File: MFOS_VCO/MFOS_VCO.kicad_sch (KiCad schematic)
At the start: 115 parts, among them J1 PWR, J10 AudioJack2, J11 AudioJack2, J12 Conn_01x01, J13 Conn_01x01, J14 Conn_01x01, J15 Conn_01x01, J16 Conn_01x01, J17 Conn_01x01, J18 Conn_01x01, J19 Conn_01x01, J2 AudioJack2, J21 Conn_01x01, J23 Conn_01x01, J25 Conn_01x01, J3 AudioJack2, J4 AudioJack2, J5 AudioJack2, J6 AudioJack2, J7 AudioJack2, J8 AudioJack2, J9 AudioJack2, Q1 PN4391, U1 OP275, U2 TL072, U3 SSM2212, U4 TL074, U5 LM13700, U6 TL072, U7 TL071

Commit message: Reviewed BOM
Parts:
- C12: value 0.1u -> 1u; symbol Device:C_Polarized -> dhk:C_Tantalum
- C13: symbol Device:C_Polarized -> dhk:C_Tantalum
- C6: symbol Device:C -> dhk:R_Potentiometer_Trim_Top
- D1, D2, D3, D4, D5, D6, D7, D8: value D -> 1N914; footprint (none) -> Diode_THT:D_DO-35_SOD27_P7.62mm_Horizontal; symbol Device:D -> Diode:1N914
- J1, J12, J13, J14, J15, J16, J17, J18, J19, J21, J23, J25: now left out of the parts list
- J10, J11, J2, J3, J4, J5, J6, J7, J8, J9: symbol Connector:AudioJack2 -> Connector:Jack-DC
- R11, R16, R5, R59, R60, R64, R7: symbol Device:R_Potentiometer -> dhk:R_Potentiometer_Trim_Top
- R24: value 2k -> 1.5k
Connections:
- net CV1: now also J2.2; no longer J2.T
- net CV2: now also J3.2; no longer J3.T
- net CV3: now also J4.2; no longer J4.T
- net GND: now also J10.1, J11.1, J8.1, J9.1; no longer J10.S, J11.S, J8.S, J9.S
- net LIN: now also J5.2; no longer J5.T
- net PWM: now also J6.2; no longer J6.T
- net RAW: now also C6.3; no longer C6.2
- net RMP: now also J11.2; no longer J11.T
- net SIN: now also J9.2; no longer J9.T
- net SQR: now also J10.2; no longer J10.T
- net SYNC: now also J7.2; no longer J7.T
- net TRI: now also J8.2; no longer J8.T

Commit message: Designs adapted for BOM
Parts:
- C1: value 0.1u -> 0.1uF
- C10, C7: value 10u -> 10uF
- C12, C13: value 1u -> 1uF
- C14: value 0.002u -> 0.002uF
- C15, C16, C2, C8: value .1u -> 0.1uF
- C17, C3: value 100p -> 100pF
- C18: value 4.7p -> 4.7pF
- C4: value 10p -> 10pF
- C5: value 0.001u -> 0.001uF
- C6: value 0.005u -> .005uF; symbol dhk:R_Potentiometer_Trim_Top -> dhk:C_Polystyrene
- J10, J11, J2, J3, J4, J5, J6, J7, J8, J9: value AudioJack2 -> Jack-DC
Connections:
- net RAW: now also C6.2; no longer C6.3

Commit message: yeah yeah
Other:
- moved on the sheet: C1, C12, C13, C14, C15, C16, C2, C4, D2, D3, D4, D5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

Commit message: Final changes
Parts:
- removed C1, C15, C16, C2: 0.1uF, symbol Device:C
- removed C12, C13: 1uF, symbol dhk:C_Tantalum
- removed C14: 0.002uF, symbol Device:C
- removed C4: 10pF, symbol Device:C
- removed D2, D3, D4, D5, D6, D7: 1N914, Diode_THT:D_DO-35_SOD27_P7.62mm_Horizontal, symbol Diode:1N914
- removed R1, R12, R13, R25, R32, R35, R40: 10k, symbol Device:R
- removed R14, R21, R48: 20k, symbol Device:R
- removed R20: 47k, symbol Device:R
- removed R22, R26, R49, R51: 1k, symbol Device:R
- removed R29, R44, R6, R67: 100k, symbol Device:R
- removed R36, R52: 4.7k, symbol Device:R
- removed R39: 100k, symbol Device:R_Potentiometer
- removed R41: 3k, symbol Device:R
- removed R45: 1M, symbol Device:R
- removed R5, R7: 10k, symbol dhk:R_Potentiometer_Trim_Top
- removed R53: 130k, symbol Device:R
- removed R59: 1M, symbol dhk:R_Potentiometer_Trim_Top
- removed R60, R64: 100k, symbol dhk:R_Potentiometer_Trim_Top
- removed R61: 470k, symbol Device:R
- removed R68: 10M, symbol Device:R
- removed unit 1 of U4
- removed unit 4 of U4
- removed unit 3 of U4
- removed unit 2 of U4
- removed unit 2 of U5
- removed unit 1 of U5
- removed unit 3 of U5
- removed unit 4 of U5
- removed unit 2 of U6
- removed unit 1 of U6
- removed U7: TL071, symbol Amplifier_Operational:TL071
- added J20: Jack-DC, symbol Connector:Jack-DC
- added J22: Conn_01x01, symbol Connector_Generic:Conn_01x01
- added R27: 100k, symbol Device:R
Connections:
- net at C19.1, R10.2, R15.2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: now also R27.2
- net R2P1: now reaches R2.1, R71.2
- net R2P2: now reaches R10.1, R2.2
- net R3P1: now reaches R3.1, R56.2
- net R2P3: now reaches R2.3, R65.1
- net R3P3: now reaches R3.3, R57.1
- net R3P2: now reaches R3.2, R8.1
- new net CV4: J20.2, J22.1 (Pin_1), R27.1
- no-connect marks 14 -> 7
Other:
- moved on the sheet: J15, J16, J5, J6

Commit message: Lots of headway
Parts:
- removed J1: PWR, symbol Connector_Generic:Conn_02x08_Odd_Even
- added J1: Conn_02x05_Odd_Even, Connector_IDC:IDC-Header_2x05_P2.54mm_Vertical, symbol Connector_Generic:Conn_02x05_Odd_Even
- added J24, J26: Conn_01x03, Connector_PinHeader_2.54mm:PinHeader_1x03_P2.54mm_Vertical, symbol Connector_Generic:Conn_01x03
- C10, C7: footprint (none) -> Capacitor_THT:CP_Radial_D4.0mm_P1.50mm
- C17, C18, C19, C3, C5: footprint (none) -> Capacitor_THT:C_Disc_D3.4mm_W2.1mm_P2.50mm
- C6: footprint (none) -> Capacitor_THT:C_Axial_L12.0mm_D6.5mm_P15.00mm_Horizontal
- C8: footprint (none) -> Capacitor_THT:C_Disc_D5.0mm_W2.5mm_P2.50mm
- J12, J13, J14, J15, J16, J17, J18, J19, J21, J22, J23, J25: footprint (none) -> Connector_Pin:Pin_D1.0mm_L10.0mm_LooseFit
- Q1: footprint (none) -> Package_TO_SOT_THT:TO-92
- R10, R11, R15, R16, R17, R18, R19, R23, R24, R27, R28, R30, R31, R34, R42, R46, R47, R50, R56, R57, R65, R66, R69, R70, R71, R8, R9: footprint (none) -> Resistor_THT:R_Axial_DIN0207_L6.3mm_D2.5mm_P7.62mm_Horizontal
- U1, U2, U6: footprint (none) -> Package_DIP:DIP-8_W7.62mm_Socket_LongPads
- U3: footprint (none) -> Package_SO:SOIC-8_3.9x4.9mm_P1.27mm
- U4: footprint (none) -> Package_DIP:DIP-14_W7.62mm_Socket_LongPads
- U5: footprint (none) -> Package_SO:SOIC-16_3.9x9.9mm_P1.27mm
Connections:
- net +12V: now also J1.10 (Pin_10), J1.9 (Pin_9)
- net -12V: now also J1.1 (Pin_1), J1.2 (Pin_2)
- net GND: now also J1.3 (Pin_3), J1.4 (Pin_4), J1.5 (Pin_5), J1.6 (Pin_6), J1.7 (Pin_7), J1.8 (Pin_8)
- net R2P1: now also J26.1 (Pin_1)
- net R2P2: now also J26.2 (Pin_2)
- net R2P3: now also J26.3 (Pin_3)
- net R3P1: now also J24.1 (Pin_1)
- net R3P2: now also J24.2 (Pin_2)
- net R3P3: now also J24.3 (Pin_3)

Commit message: Laying out
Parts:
- removed J12, J13, J14, J22: Conn_01x01, Connector_Pin:Pin_D1.0mm_L10.0mm_LooseFit, symbol Connector_Generic:Conn_01x01
- added J12: Conn_01x04, Connector_PinHeader_2.54mm:PinHeader_1x04_P2.54mm_Vertical, symbol Connector_Generic:Conn_01x04
- R11, R16: footprint Resistor_THT:R_Axial_DIN0207_L6.3mm_D2.5mm_P7.62mm_Horizontal -> Potentiometer_THT:Potentiometer_Bourns_3339P_Vertical
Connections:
- net CV1: now also J12.1 (Pin_1)
- net CV2: now also J12.2 (Pin_2)
- net CV3: now also J12.3 (Pin_3)
- net CV4: now also J12.4 (Pin_4)
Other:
- moved on the sheet: J2, J20, J3, J4

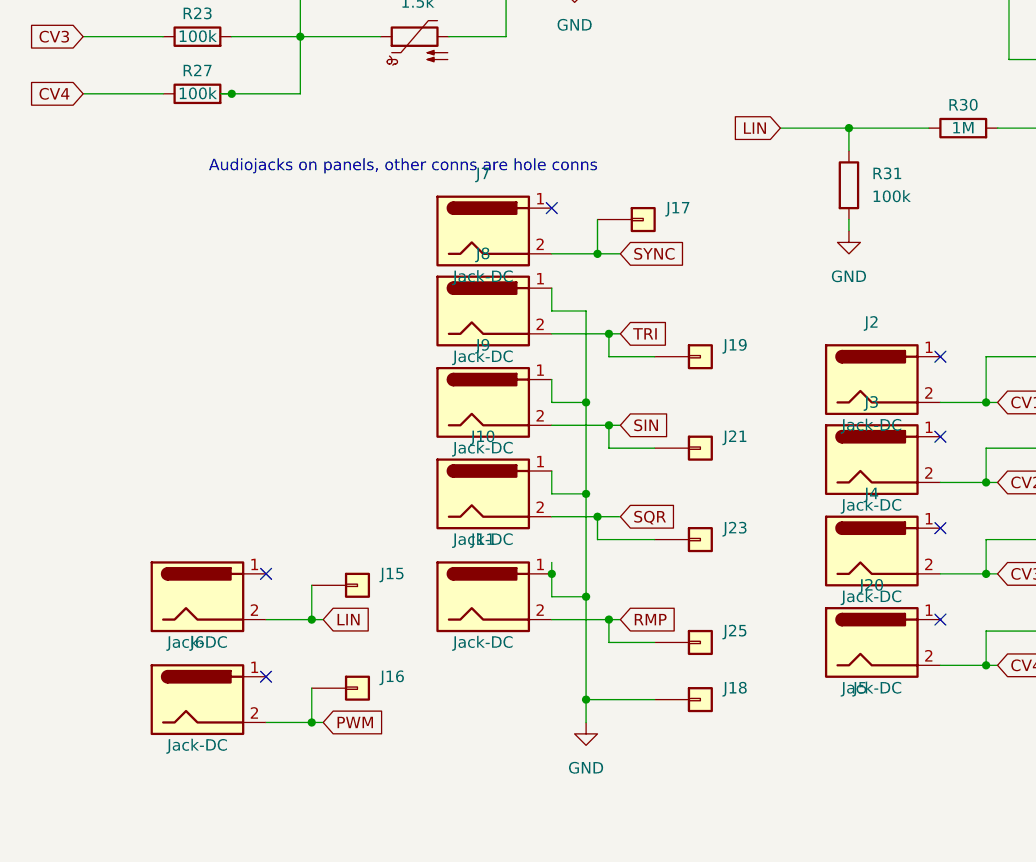
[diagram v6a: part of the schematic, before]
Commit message: Laid out last part of sheet 1
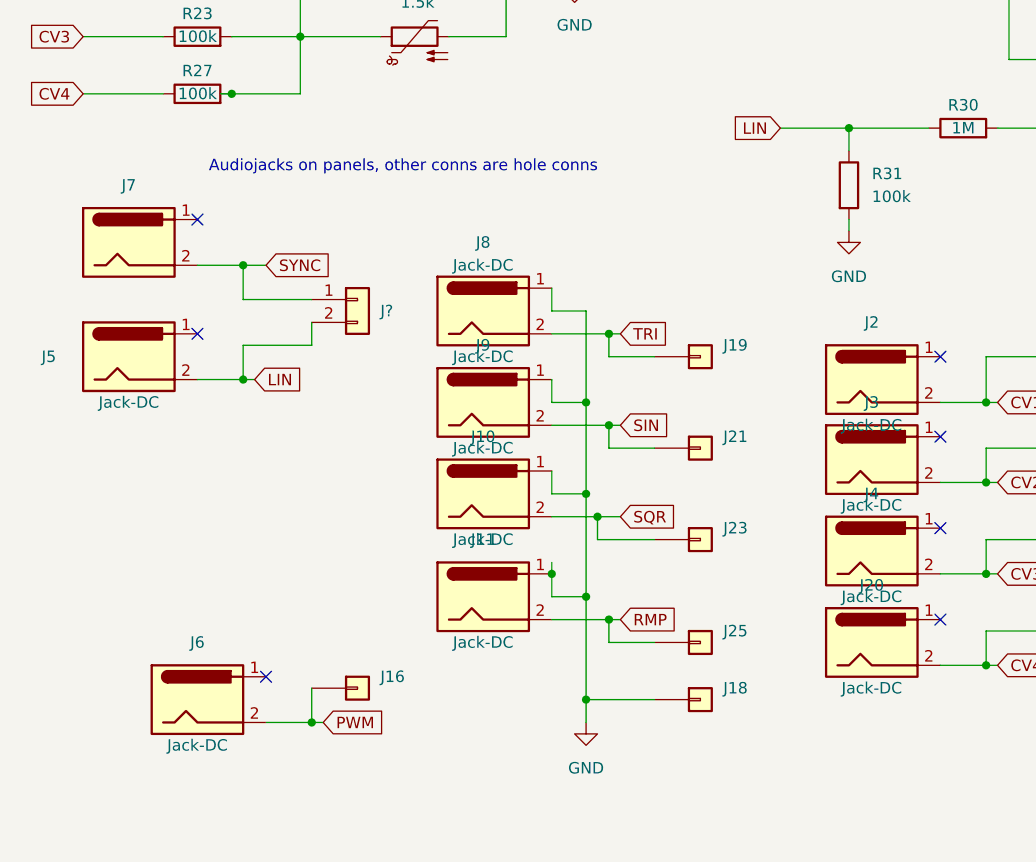
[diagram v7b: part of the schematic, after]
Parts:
- removed J15, J17: Conn_01x01, Connector_Pin:Pin_D1.0mm_L10.0mm_LooseFit, symbol Connector_Generic:Conn_01x01
- added J?: Conn_01x02, symbol Connector_Generic:Conn_01x02
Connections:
- net LIN: now also J?.2 (Pin_2)
- net SYNC: now also J?.1 (Pin_1)
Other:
- moved on the sheet: J5, J7
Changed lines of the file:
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@@
   (junction (at 55.88 34.29) (diameter 0) (color 0 0 0 0)
   )
-  (junction (at 90.17 128.27) (diameter 0) (color 0 0 0 0)
+  (junction (at 50.8 129.54) (diameter 0) (color 0 0 0 0)
   )
   (junction (at 123.19 19.05) (diameter 0) (color 0 0 0 0)
@@
   (junction (at 133.35 153.67) (diameter 0) (color 0 0 0 0)
   )
-  (junction (at 58.42 168.91) (diameter 0) (color 0 0 0 0)
+  (junction (at 50.8 142.24) (diameter 0) (color 0 0 0 0)
   )
   (junction (at 205.74 120.65) (diameter 0) (color 0 0 0 0)
@@
   )
   (no_connect (at 128.27 168.91))
-  (no_connect (at 85.09 123.19))
+  (no_connect (at 45.72 124.46))
   (no_connect (at 53.34 175.26))
-  (no_connect (at 53.34 163.83))
+  (no_connect (at 45.72 137.16))
   (no_connect (at 128.27 139.7))
   (no_connect (at 128.27 158.75))
@@
     (stroke (width 0) (type default) (color 0 0 0 0))
   )
+  (wire (pts (xy 58.42 138.43) (xy 58.42 135.89))
+    (stroke (width 0) (type default) (color 0 0 0 0))
+  )
   (wire (pts (xy 91.44 171.45) (xy 96.52 171.45))
     (stroke (width 0) (type default) (color 0 0 0 0))
@@
     (stroke (width 0) (type default) (color 0 0 0 0))
   )
-  (wire (pts (xy 53.34 168.91) (xy 58.42 168.91))
+  (wire (pts (xy 45.72 142.24) (xy 50.8 142.24))
     (stroke (width 0) (type default) (color 0 0 0 0))
   )
@@
     (stroke (width 0) (type default) (color 0 0 0 0))
   )
+  (wire (pts (xy 50.8 138.43) (xy 58.42 138.43))
+    (stroke (width 0) (type default) (color 0 0 0 0))
+  )
   (wire (pts (xy 128.27 173.99) (xy 133.35 173.99))
     (stroke (width 0) (type default) (color 0 0 0 0))
@@
     (stroke (width 0) (type default) (color 0 0 0 0))
   )
-  (wire (pts (xy 58.42 168.91) (xy 59.69 168.91))
+  (wire (pts (xy 50.8 142.24) (xy 52.07 142.24))
     (stroke (width 0) (type default) (color 0 0 0 0))
   )
@@
     (stroke (width 0) (type default) (color 0 0 0 0))
   )
-  (wire (pts (xy 90.17 128.27) (xy 92.71 128.27))
+  (wire (pts (xy 50.8 129.54) (xy 53.34 129.54))
     (stroke (width 0) (type default) (color 0 0 0 0))
   )
@@
     (stroke (width 0) (type default) (color 0 0 0 0))
   )
-  (wire (pts (xy 85.09 128.27) (xy 90.17 128.27))
+  (wire (pts (xy 45.72 129.54) (xy 50.8 129.54))
     (stroke (width 0) (type default) (color 0 0 0 0))
   )
@@
     (stroke (width 0) (type default) (color 0 0 0 0))
   )
-  (wire (pts (xy 58.42 165.1) (xy 58.42 168.91))
+  (wire (pts (xy 50.8 138.43) (xy 50.8 142.24))
     (stroke (width 0) (type default) (color 0 0 0 0))
   )
@@
     (stroke (width 0) (type default) (color 0 0 0 0))
   )
+  (wire (pts (xy 50.8 129.54) (xy 50.8 133.35))
+    (stroke (width 0) (type default) (color 0 0 0 0))
+  )
   (wire (pts (xy 171.45 72.39) (xy 151.13 72.39))
     (stroke (width 0) (type default) (color 0 0 0 0))
@@
     (stroke (width 0) (type default) (color 0 0 0 0))
   )
-  (wire (pts (xy 90.17 124.46) (xy 90.17 128.27))
-    (stroke (width 0) (type default) (color 0 0 0 0))
-  )
   (wire (pts (xy 119.38 63.5) (xy 132.08 63.5))
     (stroke (width 0) (type default) (color 0 0 0 0))
@@
   )
   (wire (pts (xy 58.42 180.34) (xy 59.69 180.34))
+    (stroke (width 0) (type default) (color 0 0 0 0))
+  )
+  (wire (pts (xy 50.8 133.35) (xy 58.42 133.35))
     (stroke (width 0) (type default) (color 0 0 0 0))
   )
@@
     )
   )
-  (global_label "LIN" (shape input) (at 59.69 168.91 0) (fields_autoplaced)
+  (global_label "LIN" (shape input) (at 52.07 142.24 0) (fields_autoplaced)
     (effects (font (size 1.27 1.27)) (justify left))
-    (property "Intersheet References" "${INTERSHEET_REFS}" (id 0) (at 65.0664 168.8306 0)
+    (property "Intersheet References" "${INTERSHEET_REFS}" (id 0) (at 57.4464 142.1606 0)
       (effects (font (size 1.27 1.27)) (justify left) hide)
     )
@@
     )
   )
-  (global_label "SYNC" (shape input) (at 92.71 128.27 0) (fields_autoplaced)
+  (global_label "SYNC" (shape input) (at 53.34 129.54 0) (fields_autoplaced)
     (effects (font (size 1.27 1.27)) (justify left))
-    (property "Intersheet References" "${INTERSHEET_REFS}" (id 0) (at 100.0217 128.1906 0)
+    (property "Intersheet References" "${INTERSHEET_REFS}" (id 0) (at 60.6517 129.4606 0)
       (effects (font (size 1.27 1.27)) (justify left) hide)
     )
@@
     (pin "2")
   )
+  (symbol (lib_id "Connector_Generic:Conn_01x02") (at 63.5 133.35 0) (unit 1)
+    (in_bom yes) (on_board yes) (fields_autoplaced)
+    (property "Reference" "J?" (id 0) (at 66.04 134.6199 0)
+      (effects (font (size 1.27 1.27)) (justify left))
+    )
+    (property "Value" "Conn_01x02" (id 1) (at 66.04 135.8899 0)
+      (effects (font (size 1.27 1.27)) (justify left) hide)
+    )
+    (property "Footprint" "" (id 2) (at 63.5 133.35 0)
+      (effects (font (size 1.27 1.27)) hide)
+    )
+    (property "Datasheet" "~" (id 3) (at 63.5 133.35 0)
+      (effects (font (size 1.27 1.27)) hide)
+    )
+    (pin "1")
+    (pin "2")
+  )
   (symbol (lib_id "power:GND") (at 213.36 86.36 0) (unit 1)
     (in_bom yes) (on_board yes) (fields_autoplaced)
@@
     (pin "2")
   )
-  (symbol (lib_id "Connector:Jack-DC") (at 45.72 166.37 0) (unit 1)
+  (symbol (lib_id "Connector:Jack-DC") (at 38.1 139.7 0) (unit 1)
     (in_bom yes) (on_board no)
-    (property "Reference" "J5" (id 0) (at 119.38 176.53 0))
-    (property "Value" "Jack-DC" (id 1) (at 45.72 171.45 0))
-    (property "Footprint" "" (id 2) (at 46.99 167.386 0)
-      (effects (font (size 1.27 1.27)) hide)
-    )
-    (property "Datasheet" "~" (id 3) (at 46.99 167.386 0)
+    (property "Reference" "J5" (id 0) (at 29.21 139.7 0))
+    (property "Value" "Jack-DC" (id 1) (at 38.1 144.78 0))
+    (property "Footprint" "" (id 2) (at 39.37 140.716 0)
+      (effects (font (size 1.27 1.27)) hide)
+    )
+    (property "Datasheet" "~" (id 3) (at 39.37 140.716 0)
       (effects (font (size 1.27 1.27)) hide)
     )
@@
   (symbol (lib_id "Connector:Jack-DC") (at 77.47 134.62 0) (unit 1)
     (in_bom yes) (on_board no)
-    (property "Reference" "J8" (id 0) (at 77.47 128.27 0))
+    (property "Reference" "J8" (id 0) (at 77.47 127 0))
     (property "Value" "Jack-DC" (id 1) (at 77.47 139.7 0))
     (property "Footprint" "" (id 2) (at 78.74 135.636 0)
@@
     (pin "1")
   )
-  (symbol (lib_id "Connector_Generic:Conn_01x01") (at 63.5 165.1 0) (unit 1)
-    (in_bom no) (on_board yes) (fields_autoplaced)
-    (property "Reference" "J15" (id 0) (at 66.04 163.8299 0)
-      (effects (font (size 1.27 1.27)) (justify left))
-    )
-    (property "Value" "Conn_01x01" (id 1) (at 66.04 166.3699 0)
-      (effects (font (size 1.27 1.27)) (justify left) hide)
-    )
-    (property "Footprint" "Connector_Pin:Pin_D1.0mm_L10.0mm_LooseFit" (id 2) (at 63.5 165.1 0)
-      (effects (font (size 1.27 1.27)) hide)
-    )
-    (property "Datasheet" "~" (id 3) (at 63.5 165.1 0)
-      (effects (font (size 1.27 1.27)) hide)
-    )
-    (pin "1")
-  )
   (symbol (lib_id "Amplifier_Operational:TL072") (at 242.57 106.68 0) (unit 2)
     (in_bom yes) (on_board yes)
@@
     (pin "1")
   )
-  (symbol (lib_id "Connector:Jack-DC") (at 77.47 125.73 0) (unit 1)
+  (symbol (lib_id "Connector:Jack-DC") (at 38.1 127 0) (unit 1)
     (in_bom yes) (on_board no)
-    (property "Reference" "J7" (id 0) (at 77.47 119.38 0))
-    (property "Value" "Jack-DC" (id 1) (at 77.47 130.81 0))
-    (property "Footprint" "" (id 2) (at 78.74 126.746 0)
-      (effects (font (size 1.27 1.27)) hide)
-    )
-    (property "Datasheet" "~" (id 3) (at 78.74 126.746 0)
-      (effects (font (size 1.27 1.27)) hide)
-    )
-    (pin "1")
-    (pin "2")
-  )
-  (symbol (lib_id "Connector_Generic:Conn_01x01") (at 95.25 124.46 0) (unit 1)
-    (in_bom no) (on_board yes) (fields_autoplaced)
-    (property "Reference" "J17" (id 0) (at 97.79 123.1899 0)
-      (effects (font (size 1.27 1.27)) (justify left))
-    )
-    (property "Value" "Conn_01x01" (id 1) (at 97.79 125.7299 0)
-      (effects (font (size 1.27 1.27)) (justify left) hide)
-    )
-    (property "Footprint" "Connector_Pin:Pin_D1.0mm_L10.0mm_LooseFit" (id 2) (at 95.25 124.46 0)
-      (effects (font (size 1.27 1.27)) hide)
-    )
-    (property "Datasheet" "~" (id 3) (at 95.25 124.46 0)
-      (effects (font (size 1.27 1.27)) hide)
-    )
-    (pin "1")
+    (property "Reference" "J7" (id 0) (at 38.1 120.65 0))
+    (property "Value" "Jack-DC" (id 1) (at 77.47 129.54 0))
+    (property "Footprint" "" (id 2) (at 39.37 128.016 0)
+      (effects (font (size 1.27 1.27)) hide)
+    )
+    (property "Datasheet" "~" (id 3) (at 39.37 128.016 0)
+      (effects (font (size 1.27 1.27)) hide)
+    )
+    (pin "1")
+    (pin "2")
   )
   (symbol (lib_id "Amplifier_Operational:TL072") (at 140.97 26.67 0) (unit 3)
@@
       (reference "J12") (unit 1) (value "Conn_01x04") (footprint "Connector_PinHeader_2.54mm:PinHeader_1x04_P2.54mm_Vertical")
     )
-    (path "/72a9e418-3b01-43de-a6a8-dec4c58dc825"
-      (reference "J15") (unit 1) (value "Conn_01x01") (footprint "Connector_Pin:Pin_D1.0mm_L10.0mm_LooseFit")
-    )
     (path "/a7dcc341-6590-40f8-935f-8db35fb800f2"
       (reference "J16") (unit 1) (value "Conn_01x01") (footprint "Connector_Pin:Pin_D1.0mm_L10.0mm_LooseFit")
     )
-    (path "/841330eb-d725-4a2d-a7c0-5074b9c10df1"
-      (reference "J17") (unit 1) (value "Conn_01x01") (footprint "Connector_Pin:Pin_D1.0mm_L10.0mm_LooseFit")
-    )
     (path "/3c2bfecb-6f92-4a2c-a840-b905613b4678"
       (reference "J18") (unit 1) (value "Conn_01x01") (footprint "Connector_Pin:Pin_D1.0mm_L10.0mm_LooseFit")
@@
       (reference "J27") (unit 1) (value "Conn_01x03") (footprint "Connector_PinHeader_2.54mm:PinHeader_1x03_P2.54mm_Vertical")
     )
+    (path "/10837bbd-a474-4d5a-b45d-6d8d91870528"
+      (reference "J?") (unit 1) (value "Conn_01x02") (footprint "")
+    )
     (path "/56fbb28b-a938-4fe3-a621-a9279caa36f8"

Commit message: All done
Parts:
- removed J16, J18, J19, J21, J23, J25: Conn_01x01, Connector_Pin:Pin_D1.0mm_L10.0mm_LooseFit, symbol Connector_Generic:Conn_01x01
- added J14: Conn_01x02, Connector_PinHeader_2.54mm:PinHeader_1x02_P2.54mm_Vertical, symbol Connector_Generic:Conn_01x02
- added J15: Conn_01x04, Connector_PinHeader_2.54mm:PinHeader_1x04_P2.54mm_Vertical, symbol Connector_Generic:Conn_01x04
- J13: renamed from J?; footprint (none) -> Connector_PinHeader_2.54mm:PinHeader_1x02_P2.54mm_Vertical
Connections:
- net GND: now also J14.2 (Pin_2)
- net PWM: now also J14.1 (Pin_1)
- net RMP: now also J15.4 (Pin_4)
- net SIN: now also J15.2 (Pin_2)
- net SQR: now also J15.3 (Pin_3)
- net TRI: now also J15.1 (Pin_1)
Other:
- moved on the sheet: J6
